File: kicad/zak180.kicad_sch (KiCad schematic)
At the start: 10 parts, among them U11 74HC02, U16 74HC00

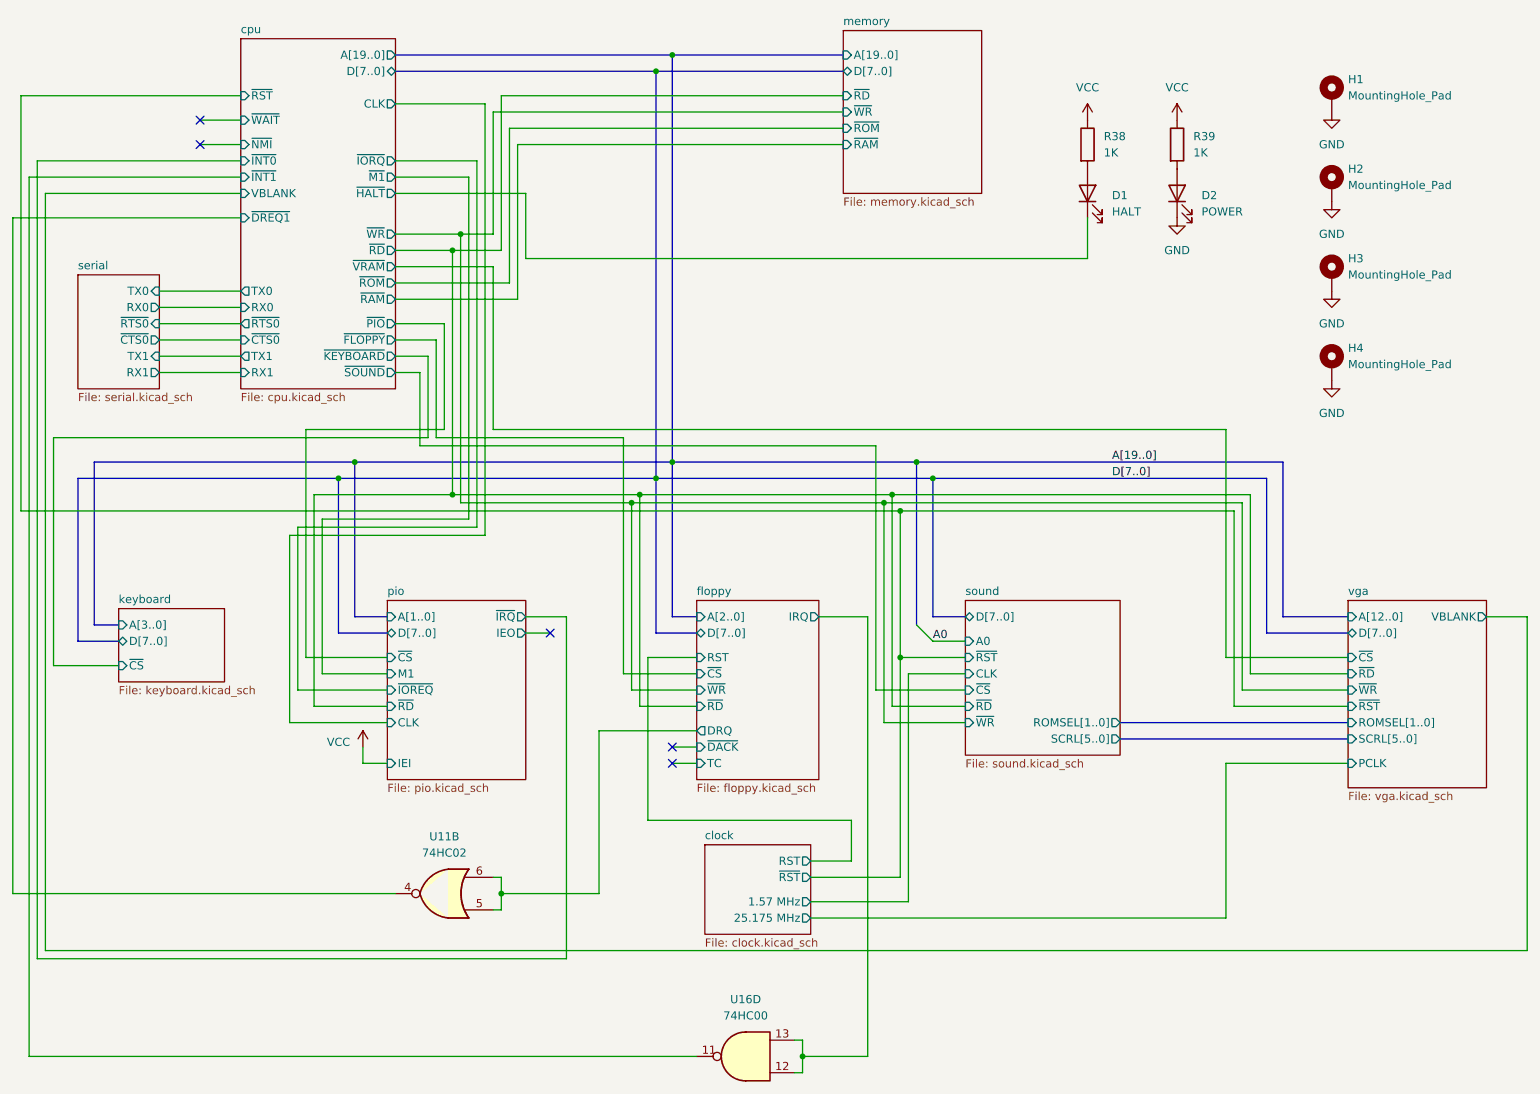
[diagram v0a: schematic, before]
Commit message: hw: simplify logic, replace some SSI with GALs
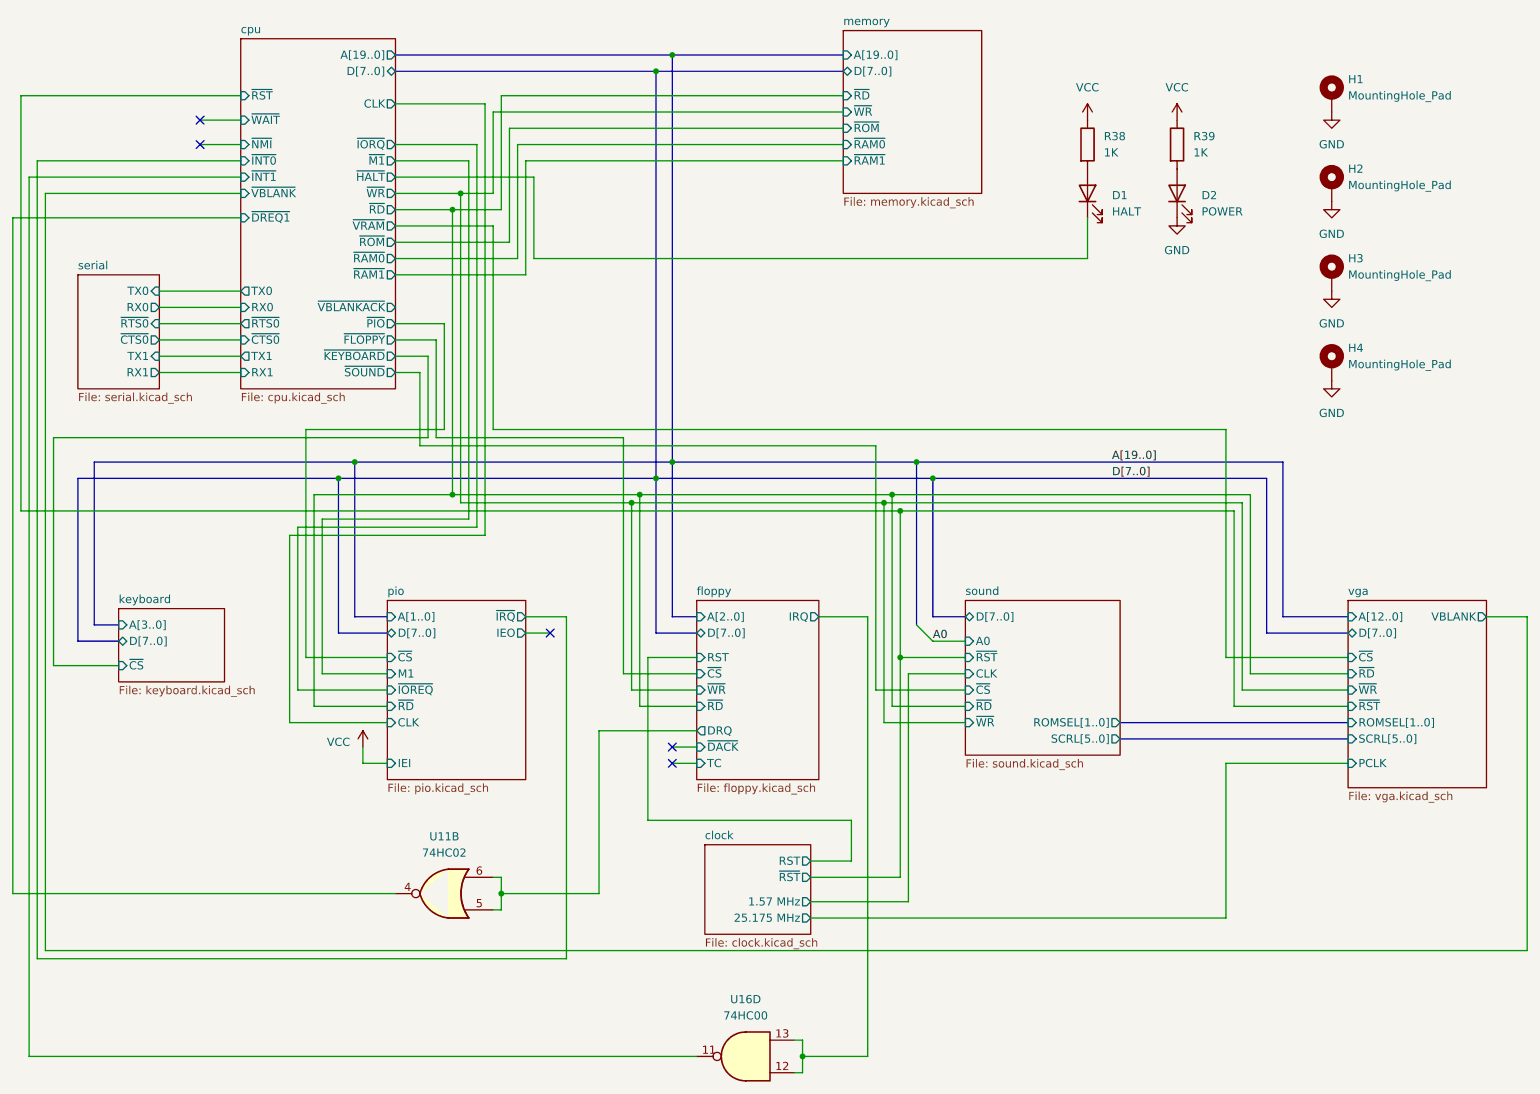
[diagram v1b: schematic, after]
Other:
- sheet cpu ports: added ~{RAM0}, ~{RAM1}, ~{VBLANKACK}, ~{VBLANK}; removed VBLANK, ~{RAM}
- sheet memory ports: added ~{RAM0}, ~{RAM1}; removed ~{RAM}
